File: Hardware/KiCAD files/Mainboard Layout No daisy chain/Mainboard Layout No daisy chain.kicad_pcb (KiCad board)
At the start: 2 copper layers, 207 x 174.8 mm, 88 parts, among them J1 JST_03, J11 Conn_01x04, J12 JST_06, J13 Conn_01x08, J14 Conn_01x08, J15 Screw_Terminal_2_P5.00mm, J17 PINHD_1x8_Male, J18 PINHD_1x8_Male, J19 PINHD_1x8_Male, J2 Screw_Terminal_2_P5.00mm, J20 PINHD_1x8_Male, J22 PINHD_1x8_Male, J23 PINHD_1x8_Male, J24 PINHD_1x8_Male, J25 Conn_01x04, J26 Conn_01x04, J27 Conn_01x04, J28 PINHD_1x8_Male, J3 Screw_Terminal_2_P3.50mm, J30 USB-A1VSB6, J31 JST_03, J32 USB-A1VSB6, J34 JST_03, J35 JST_03, J36 JST_03, J37 JST_03, J38 JST_03, J4 JST_06, J5 Conn_01x04, J6 JST_06, J7 JST_06, J8 Conn_01x06, J9 Conn_01x10, Q1 BS170, Q2 2DD1664, SW1 210-4MS, SW2 210-4MS, SW3 210-4MS, SW4 210-4MS, SW8 Push_Button, SW9 Push_Button, U1 CP2102-GM, U12 ESP32-S3-WROOM-1, U2 PCA9534PW_118, U4 PCA9534PW_118

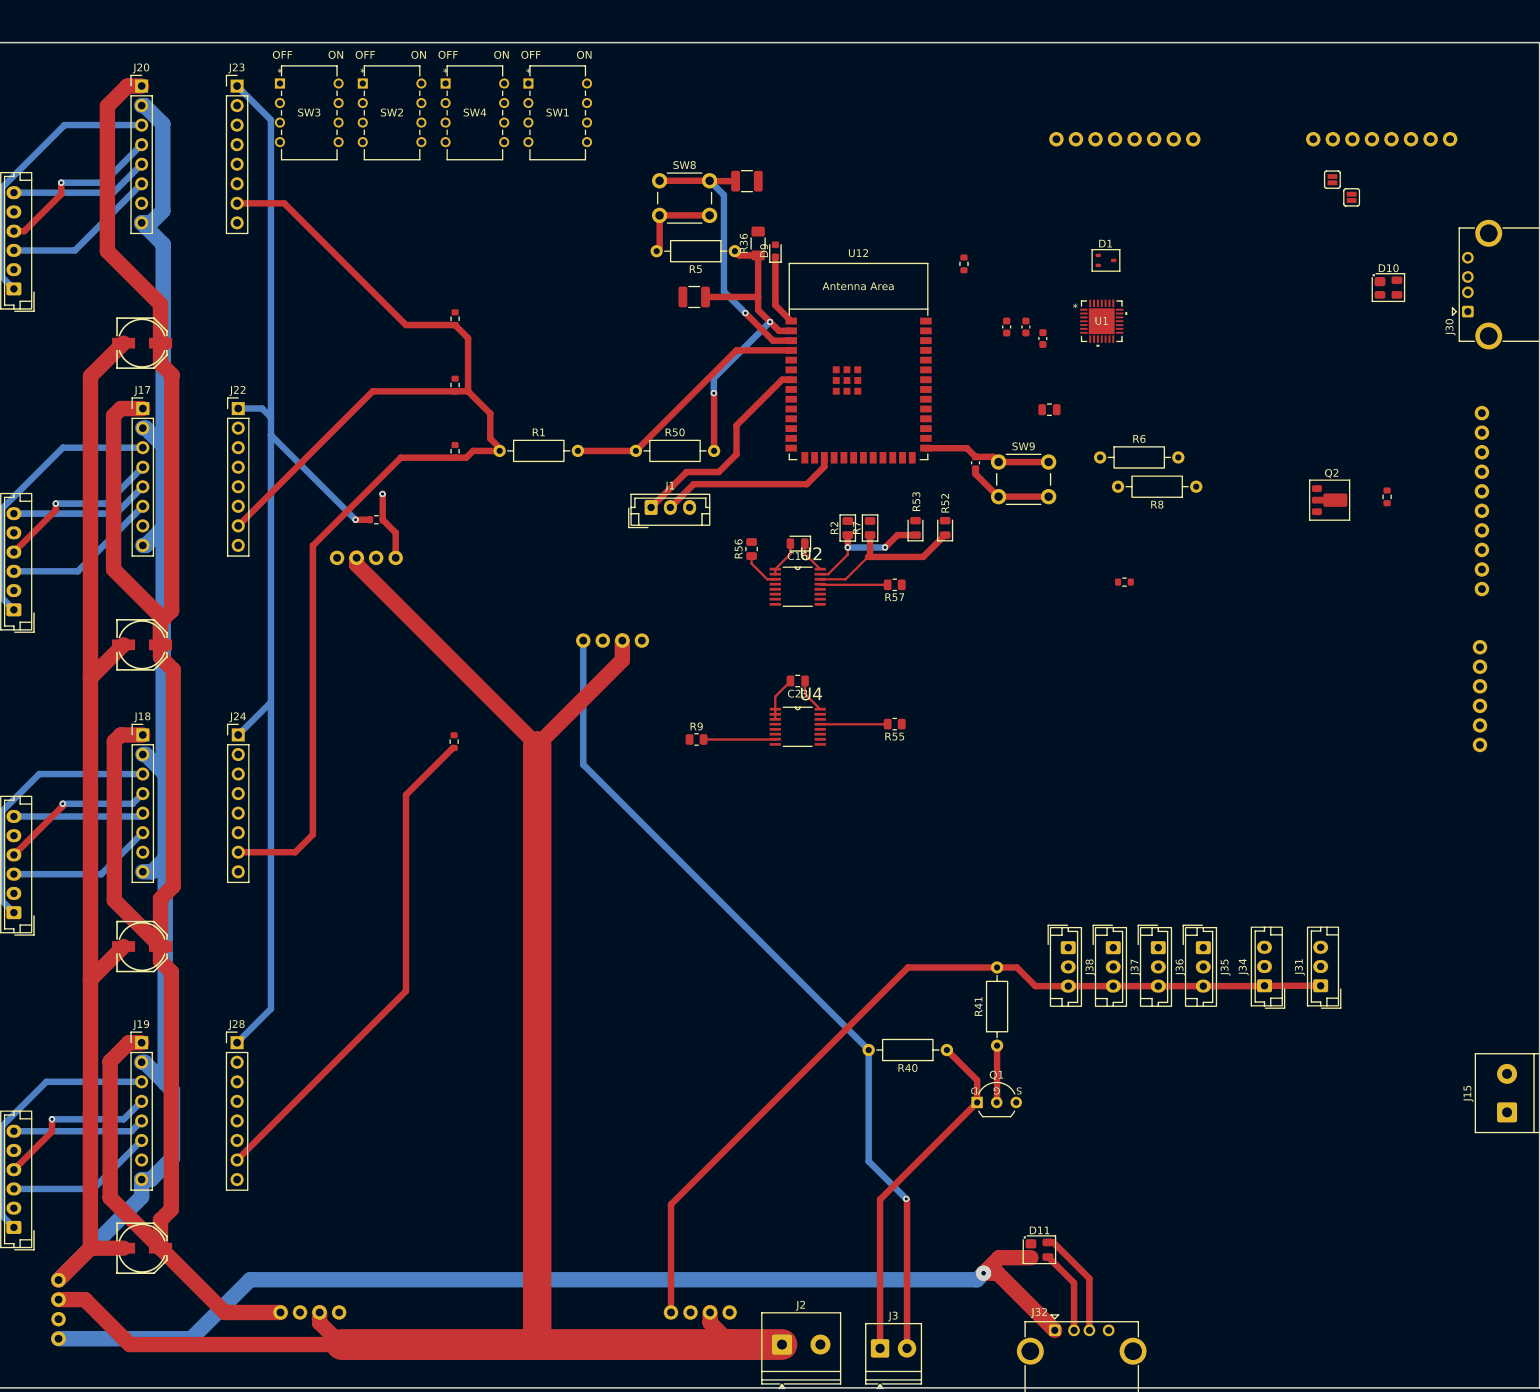
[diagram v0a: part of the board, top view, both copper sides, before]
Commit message: 1st submitted iteration
added a folder for reviewing PCB's.
fixed various smaller issues on the PCB.
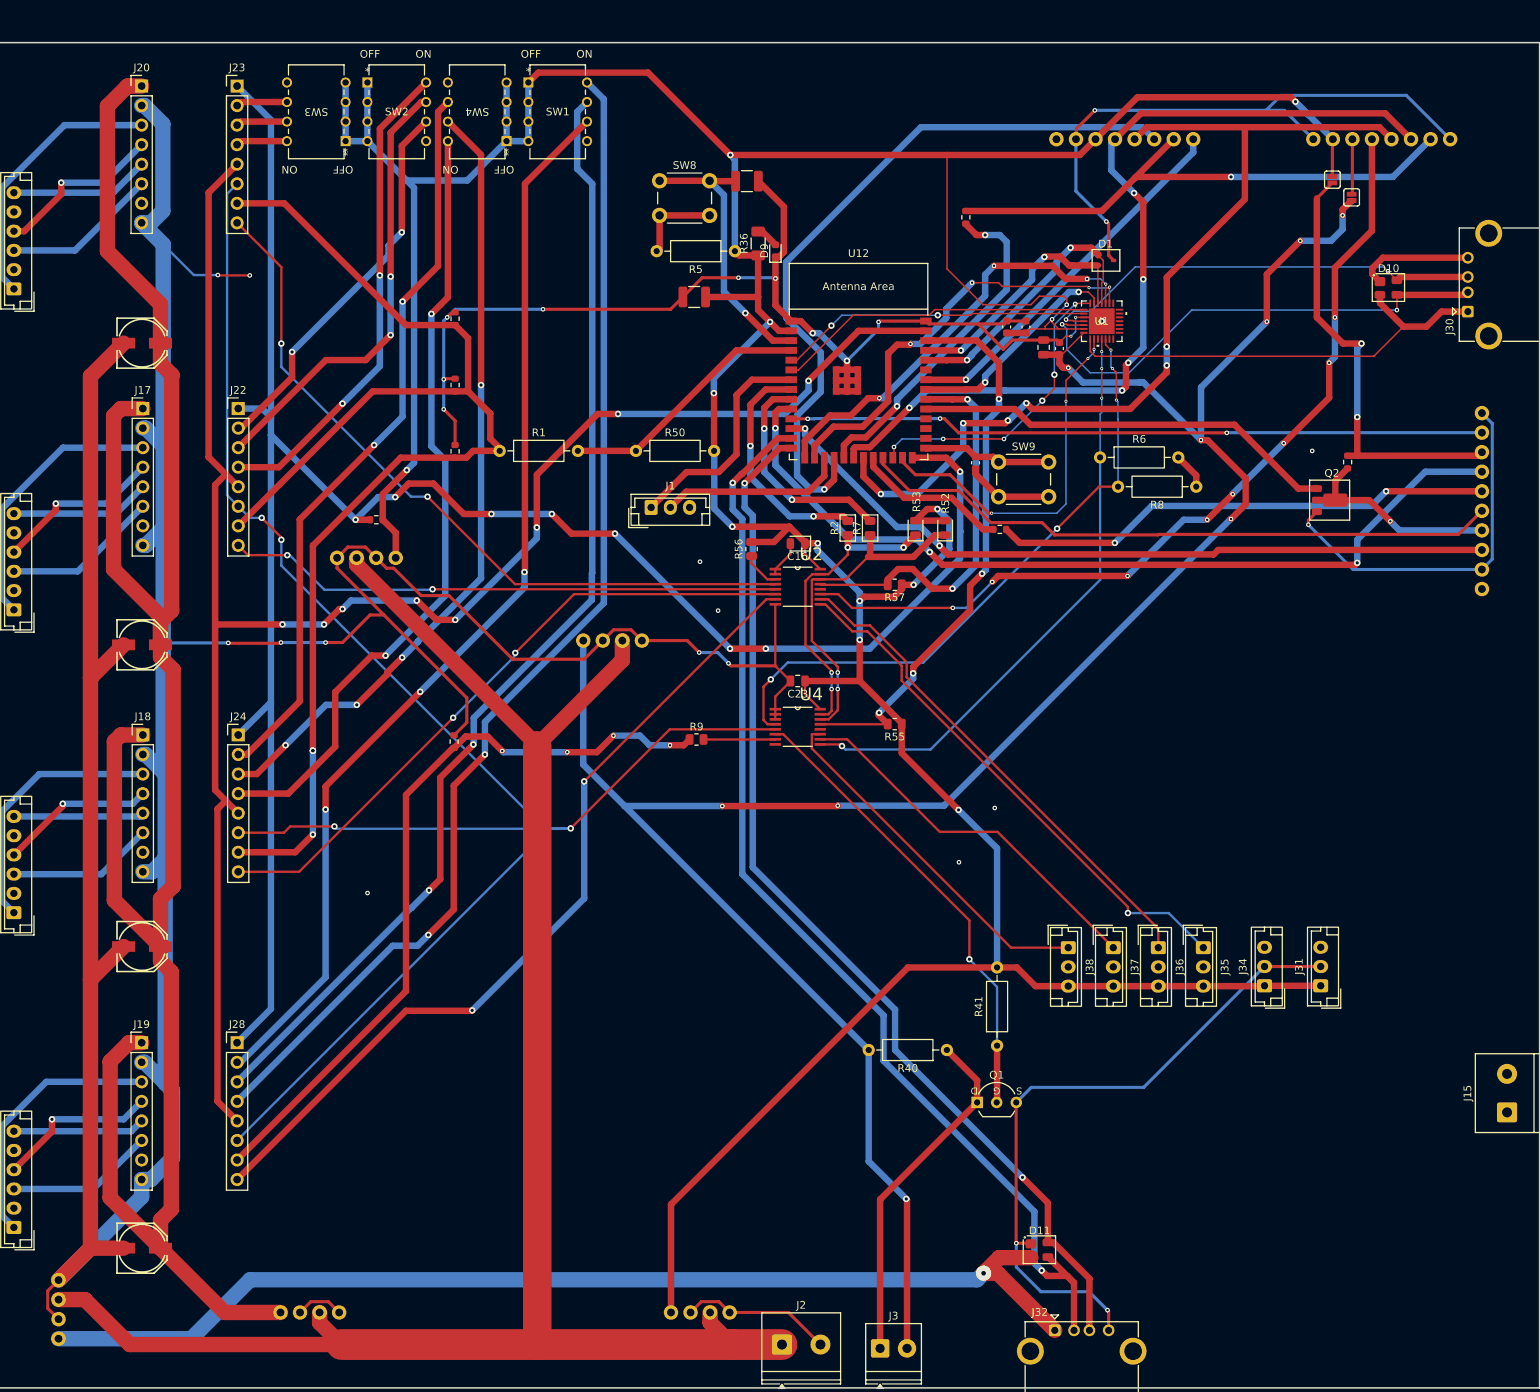
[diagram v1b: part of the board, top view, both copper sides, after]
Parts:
- removed J8: Conn_01x06, PCM_SparkFun-Connector:1x06_P2.54mm
- moved R3 17.6 mm to (177.4, 78.2)
- moved SW3 11.4 mm to (92.4, 27.8), turned to 180 degrees
- moved SW4 10.9 mm to (113.3, 27.8), turned to 180 degrees
- moved C8 8.13 mm to (183.1, 54.5), turned to 90 degrees
- moved R48 6.84 mm to (222.6, 69.5)
- moved R4 6.06 mm to (173.0, 37.6)
- moved C7 2.51 mm to (185.2, 54.7)
- moved SW2 0.62 mm to (95.2, 20.1)
- moved SW1 0.13 mm to (116.2, 20.1)
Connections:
- J13 pad 6: SPI1_0SS -> SPI1_1SS
- J14 pad 7: MOSI_1 -> MISO_1
- J9 pad 6: MOSI_4 -> MISO_4
- U12 pad 18: unconnected-(U12-GPIO10/TOUCH10/ADC1_CH9/FSPICS0/FSPIIO4/SUBSPICS0-Pad18) -> SPI1_1SS
- U12 pad 35: TFT_interrupt -> unconnected-(U12-MTMS/GPIO42-Pad35)
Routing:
- net GND: track 357.2 -> 927.6 mm, vias 0 -> 30
- net +3.3V: track 172.2 -> 642.3 mm, vias 3 -> 16
- net Reset: track 0.00 -> 249.9 mm, vias 0 -> 8
- net nSLP: track 0.00 -> 238.6 mm, vias 0 -> 4
- net +5V: track 109.4 -> 289.3 mm, vias 1 -> 9
- net MODE_0_GPIOE: track 0.00 -> 154.9 mm, vias 0 -> 2
- net MODE_1_GPIOE: track 0.00 -> 147.8 mm, vias 0 -> 2
- net MODE_2_GPIOE: track 0.00 -> 141.3 mm, vias 0 -> 3
- net PI_D-: track 11.0 -> 144.8 mm, vias 0 -> 2
- net PI_D+: track 14.1 -> 137.0 mm, vias 0 -> 2
- net MOSI_1: track 0.00 -> 122.6 mm, vias 0 -> 6
- net SPI1_CLK: track 0.00 -> 116.2 mm, vias 0 -> 5
- net SPI1_0SS: track 0.00 -> 114.1 mm, vias 0 -> 8
- net SPI4_CLK: track 0.00 -> 113.0 mm, vias 0 -> 3
- net N_ENBL: track 156.1 -> 268.7 mm, vias 1 -> 8
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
